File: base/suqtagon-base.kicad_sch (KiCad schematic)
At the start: 1 part

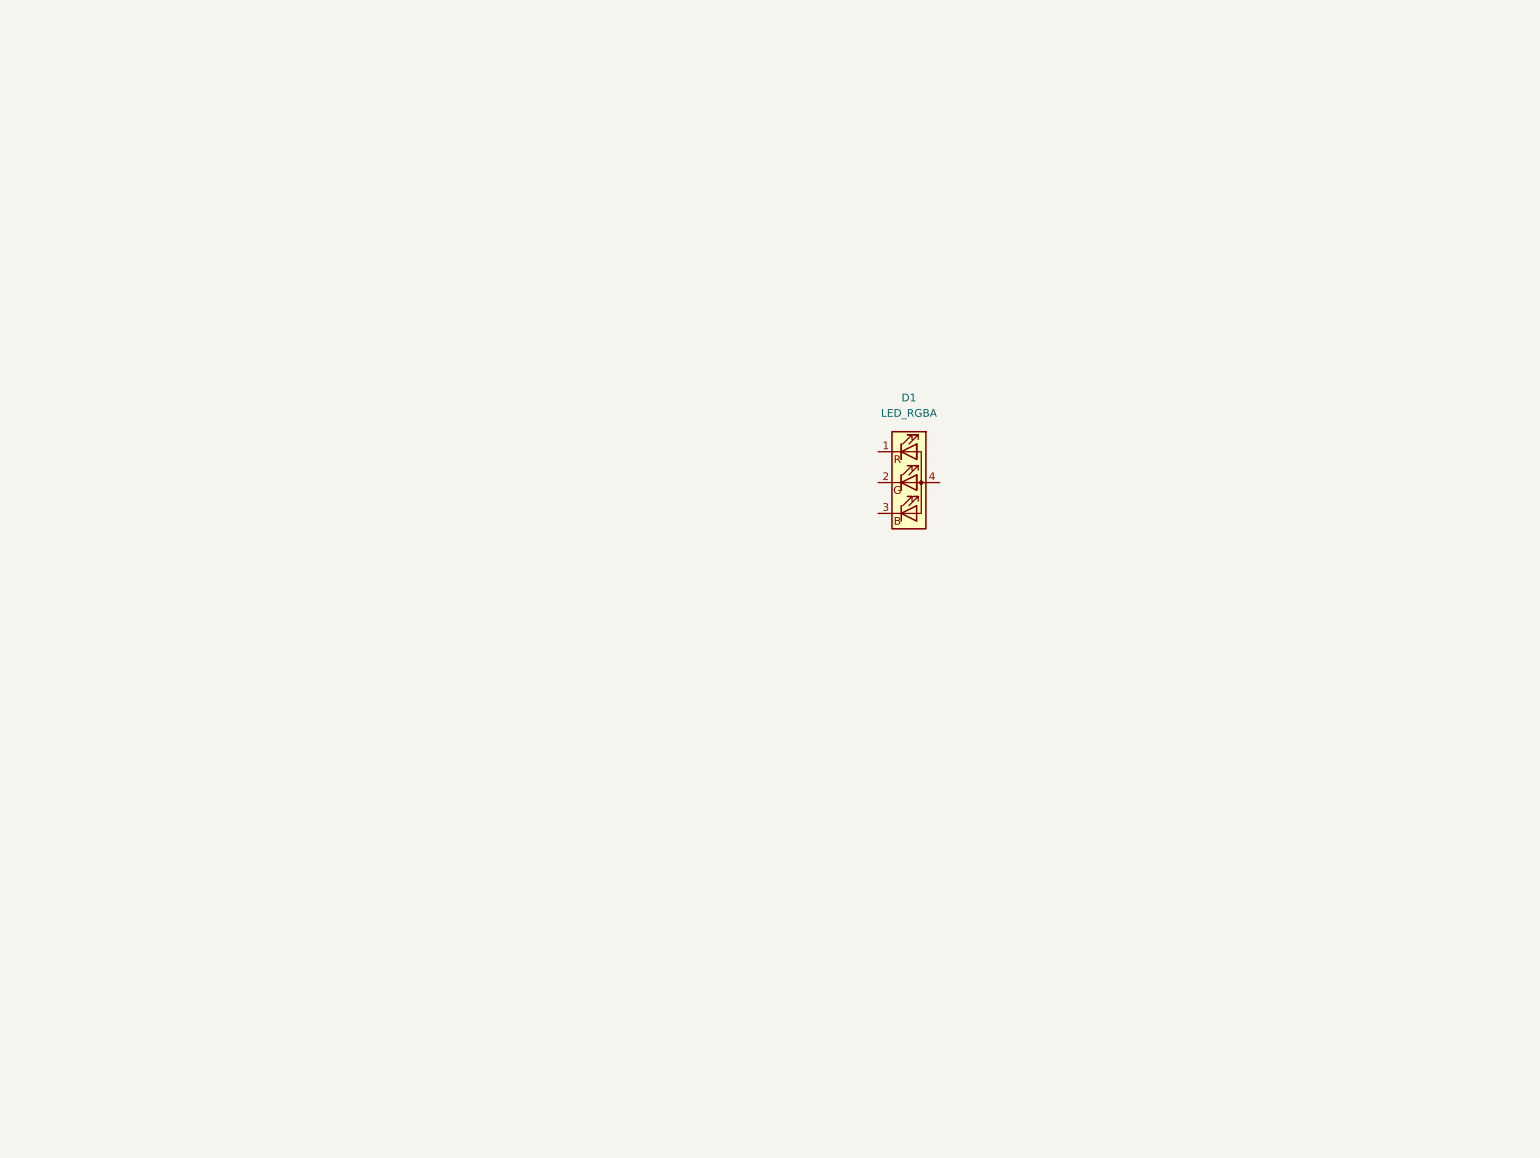
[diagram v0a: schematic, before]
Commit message: populating some components in base
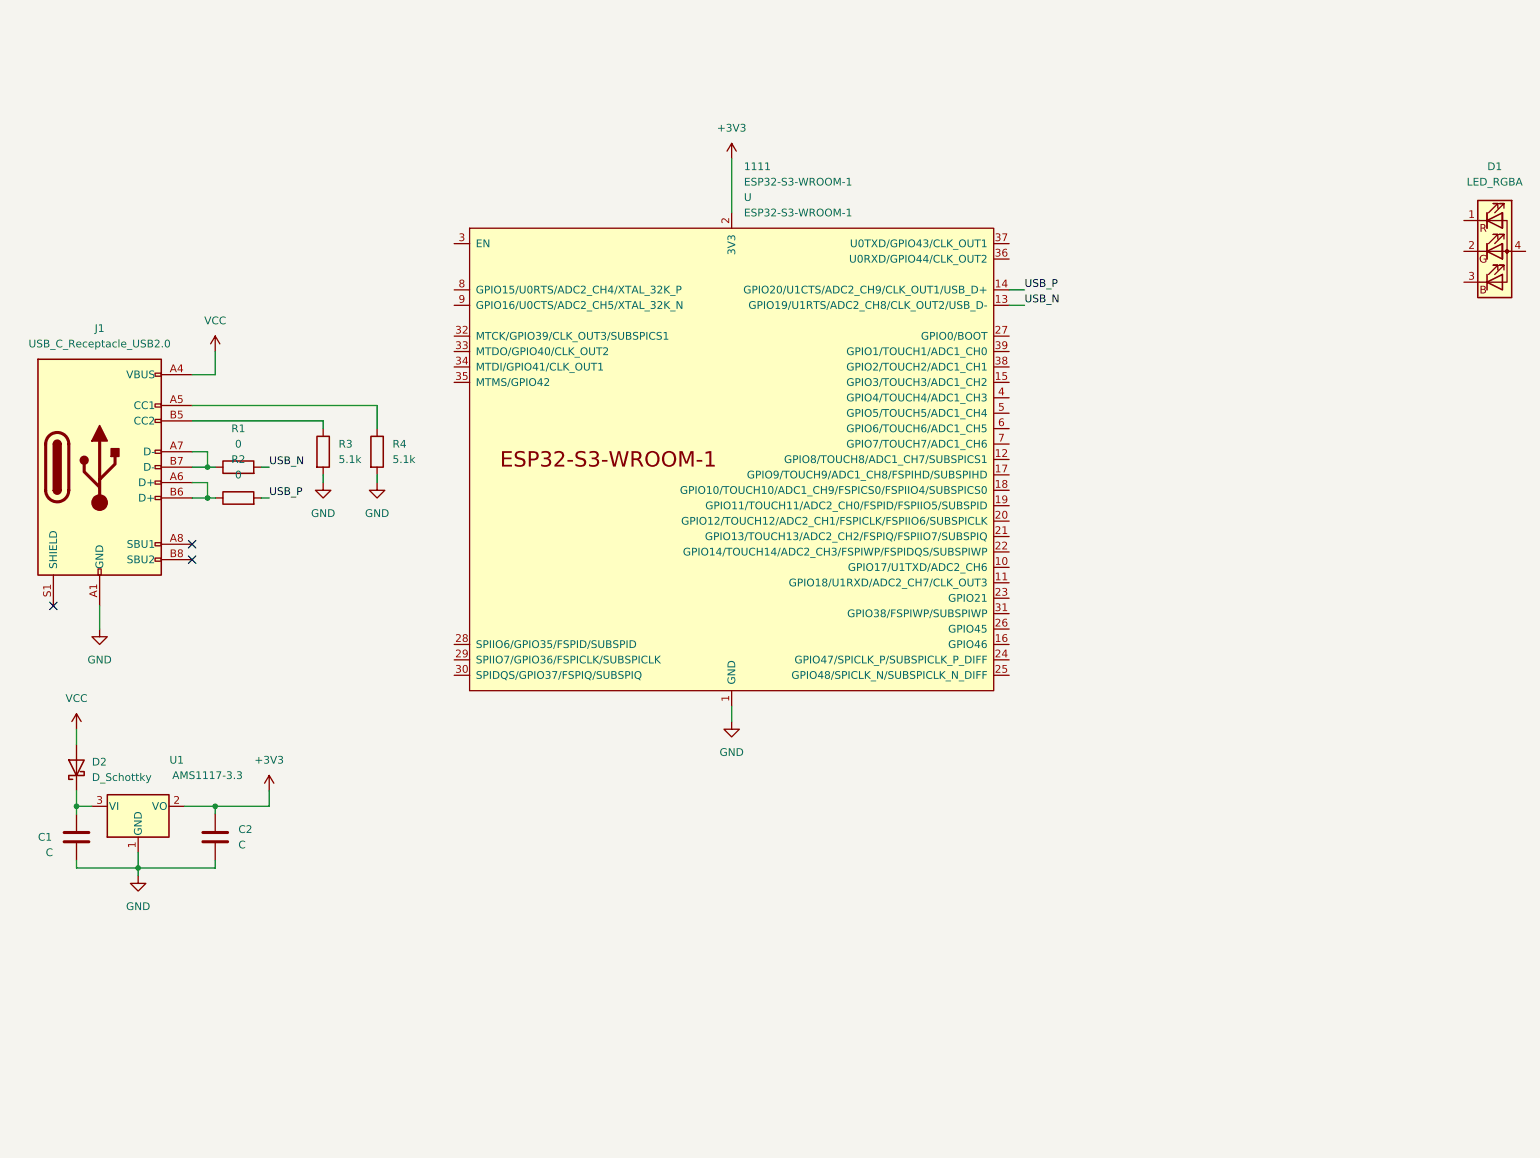
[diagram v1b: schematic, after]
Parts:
- added 1111: ESP32-S3-WROOM-1, Espressif:ESP32-S3-WROOM-1U, symbol Espressif:ESP32-S3-WROOM-1
- added C1, C2: C, Capacitor_SMD:C_0805_2012Metric_Pad1.18x1.45mm_HandSolder, symbol Device:C
- added D2: D_Schottky, Diode_SMD:D_0805_2012Metric_Pad1.15x1.40mm_HandSolder, symbol Device:D_Schottky
- added J1: USB_C_Receptacle_USB2.0, Connector_USB:USB_C_Receptacle_HRO_TYPE-C-31-M-12, symbol Connector:USB_C_Receptacle_USB2.0
- added R1, R2: 0, Resistor_SMD:R_0805_2012Metric_Pad1.20x1.40mm_HandSolder, symbol Device:R
- added R3, R4: 5.1k, Resistor_SMD:R_0805_2012Metric_Pad1.20x1.40mm_HandSolder, symbol Device:R
- added U1: AMS1117-3.3, Package_TO_SOT_SMD:SOT-223-3_TabPin2, symbol Regulator_Linear:AMS1117-3.3
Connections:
- new net: J1.B5 (CC2), R3.1
- new net: C1.1, D2.1 (K), U1.3 (VI)
- new net: J1.A6 (D+), J1.B6 (D+), R2.1
- new net: J1.A7 (D-), J1.B7 (D-), R1.1
- new net: J1.A5 (CC1), R4.1
- new net +3V3: 1111.2 (3V3), C2.1, U1.2 (VO)
- new net GND: 1111.1 (GND), 1111.40 (GND), 1111.41 (GND), C1.2, C2.2, J1.A1 (GND), J1.A12 (GND), J1.B1 (GND), J1.B12 (GND), R3.2, R4.2, U1.1 (GND)
- new net USB_N: 1111.13 (GPIO19/U1RTS/ADC2_CH8/CLK_OUT2/USB_D-), R1.2
- new net USB_P: 1111.14 (GPIO20/U1CTS/ADC2_CH9/CLK_OUT1/USB_D+), R2.2
- new net VCC: D2.2 (A), J1.A4 (VBUS), J1.A9 (VBUS), J1.B4 (VBUS), J1.B9 (VBUS)
- no-connect marks 0 -> 3
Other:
- moved on the sheet: D1

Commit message: added more esp components
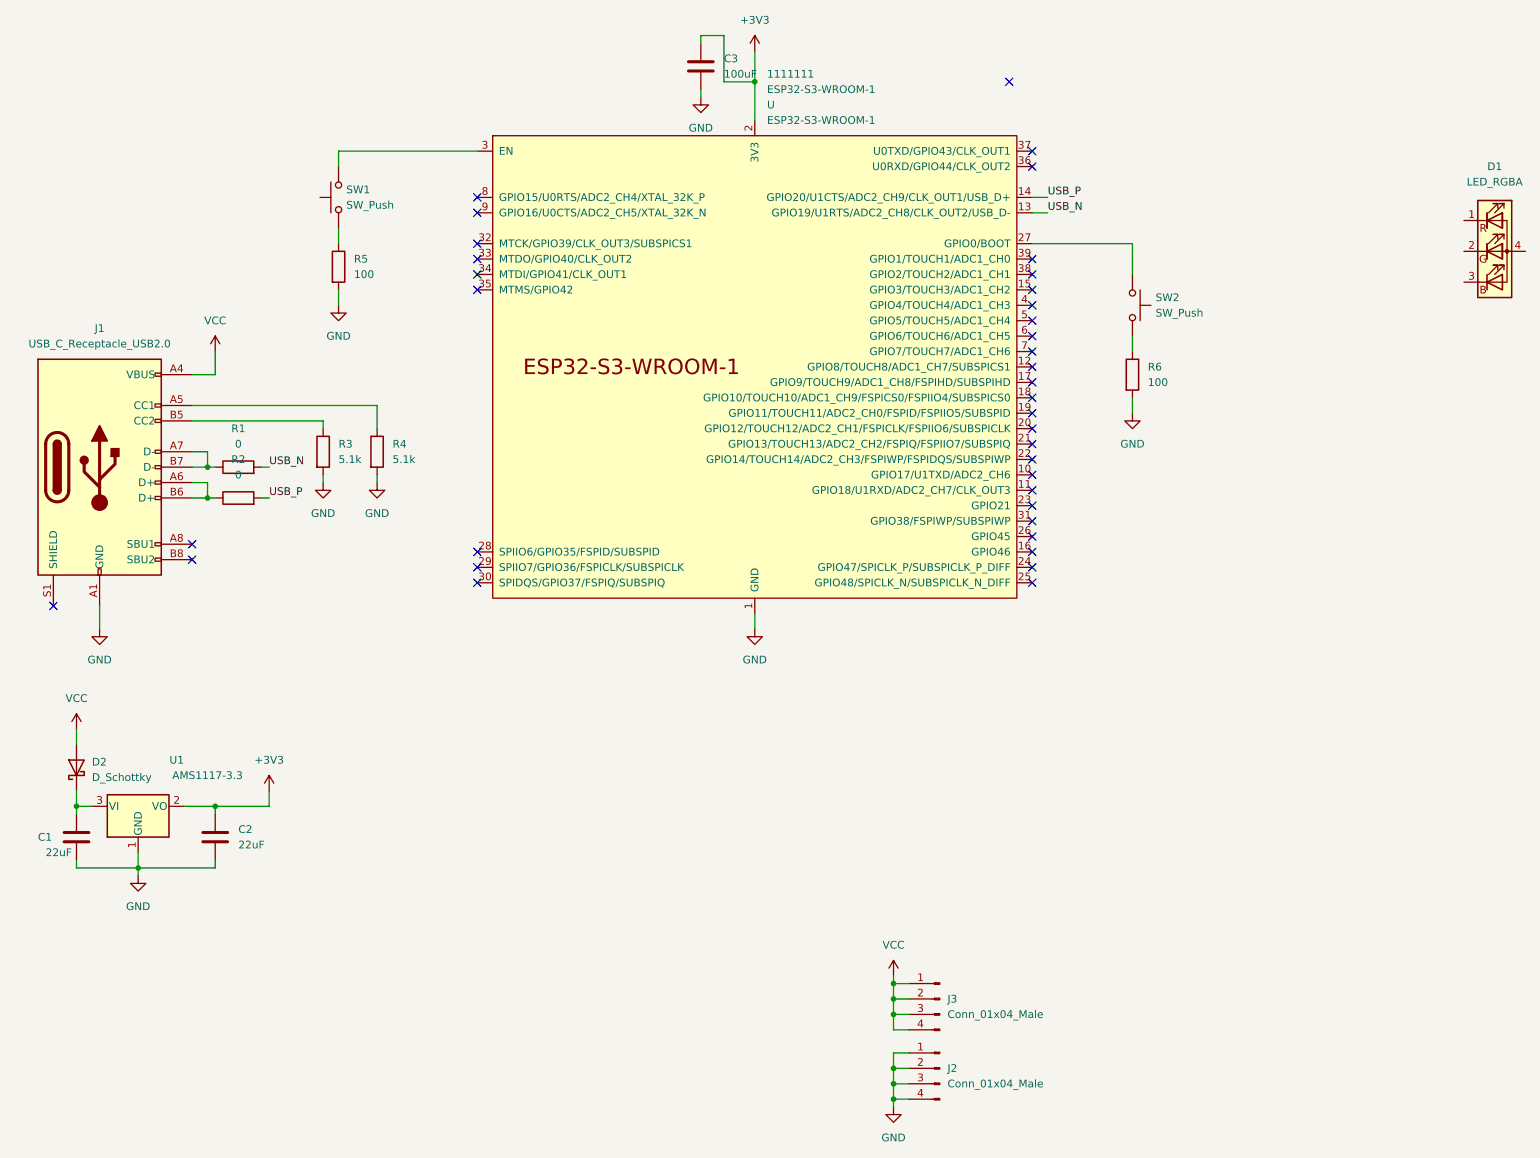
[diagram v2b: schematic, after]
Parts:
- added C3: 100uF, Capacitor_SMD:C_0805_2012Metric_Pad1.18x1.45mm_HandSolder, symbol Device:C
- added J2, J3: Conn_01x04_Male, Connector_PinHeader_2.54mm:PinHeader_2x02_P2.54mm_Vertical_SMD, symbol Connector:Conn_01x04_Male
- added R5, R6: 100, Resistor_SMD:R_0805_2012Metric_Pad1.20x1.40mm_HandSolder, symbol Device:R
- added SW1, SW2: SW_Push, Button_Switch_SMD:SW_Push_1P1T_NO_6x6mm_H9.5mm, symbol Switch:SW_Push
- C1, C2: value C -> 22uF
- renumbered 1111 to 1111111
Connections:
- net +3V3: now also C3.1
- net GND: now also C3.2, J2.1 (Pin_1), J2.2 (Pin_2), J2.3 (Pin_3), J2.4 (Pin_4), R5.2, R6.2
- net VCC: now also J3.1 (Pin_1), J3.2 (Pin_2), J3.3 (Pin_3), J3.4 (Pin_4)
- net at 1111111.27 (GPIO0/BOOT): now also SW2.1
- net at 1111111.3 (EN): now also SW1.2
- new net: R6.1, SW2.2
- new net: R5.1, SW1.1
- no-connect marks 3 -> 37
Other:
- moved on the sheet: 1111111

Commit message: added smd connectors footprint
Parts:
- removed J2, J3: Conn_01x04_Male, Connector_PinHeader_2.54mm:PinHeader_2x02_P2.54mm_Vertical_SMD, symbol Connector:Conn_01x04_Male
- added D3, D4, D5: D_Schottky, Diode_SMD:D_SMB, symbol Device:D_Schottky
- added J2, J3, J4, J5, J6: Conn_01x02_Male, Connector_XH:XH _PH_2P_1x02_P2.54mm_Horizontal, symbol Connector:Conn_01x02_Male
- D2: footprint Diode_SMD:D_0805_2012Metric_Pad1.15x1.40mm_HandSolder -> Diode_SMD:D_SMB
- renumbered 1111111 to 111111111111
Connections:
- net GND: now also D3.2 (A), D4.2 (A); no longer J1.A1 (GND), J1.A12 (GND), J1.B1 (GND), J1.B12 (GND), R3.2, R4.2
- net VCC: now also C1.1, D2.1 (K), U1.3 (VI), D5.1 (K); no longer D2.2 (A), J1.A4 (VBUS), J1.A9 (VBUS), J1.B4 (VBUS), J1.B9 (VBUS)
- new net GNDA: D4.1 (K), D5.2 (A), J1.A1 (GND), J1.A12 (GND), J1.B1 (GND), J1.B12 (GND), J2.2 (Pin_2), J3.2 (Pin_2), J4.2 (Pin_2), J5.2 (Pin_2), J6.2 (Pin_2), R3.2, R4.2
- new net VBUS: D2.2 (A), D3.1 (K), J1.A4 (VBUS), J1.A9 (VBUS), J1.B4 (VBUS), J1.B9 (VBUS), J2.1 (Pin_1), J3.1 (Pin_1), J4.1 (Pin_1), J5.1 (Pin_1), J6.1 (Pin_1)
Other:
- moved on the sheet: D2
